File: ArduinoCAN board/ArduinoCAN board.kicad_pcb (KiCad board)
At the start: 2 copper layers, 71.1 x 58.4 mm, 8 parts, among them J1 CAN1, J2 CAN2, U1 MCP2515_board

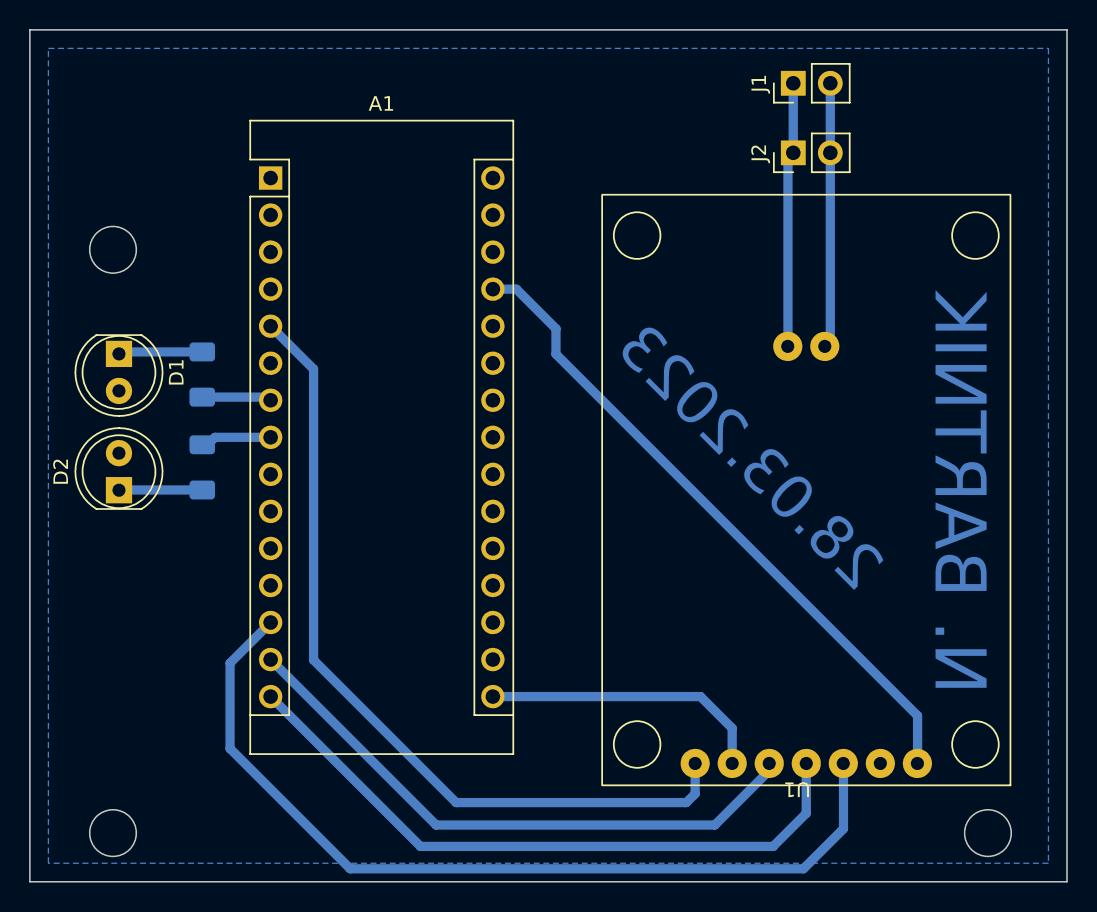
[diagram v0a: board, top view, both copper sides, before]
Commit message: added servo, pins and power connectors
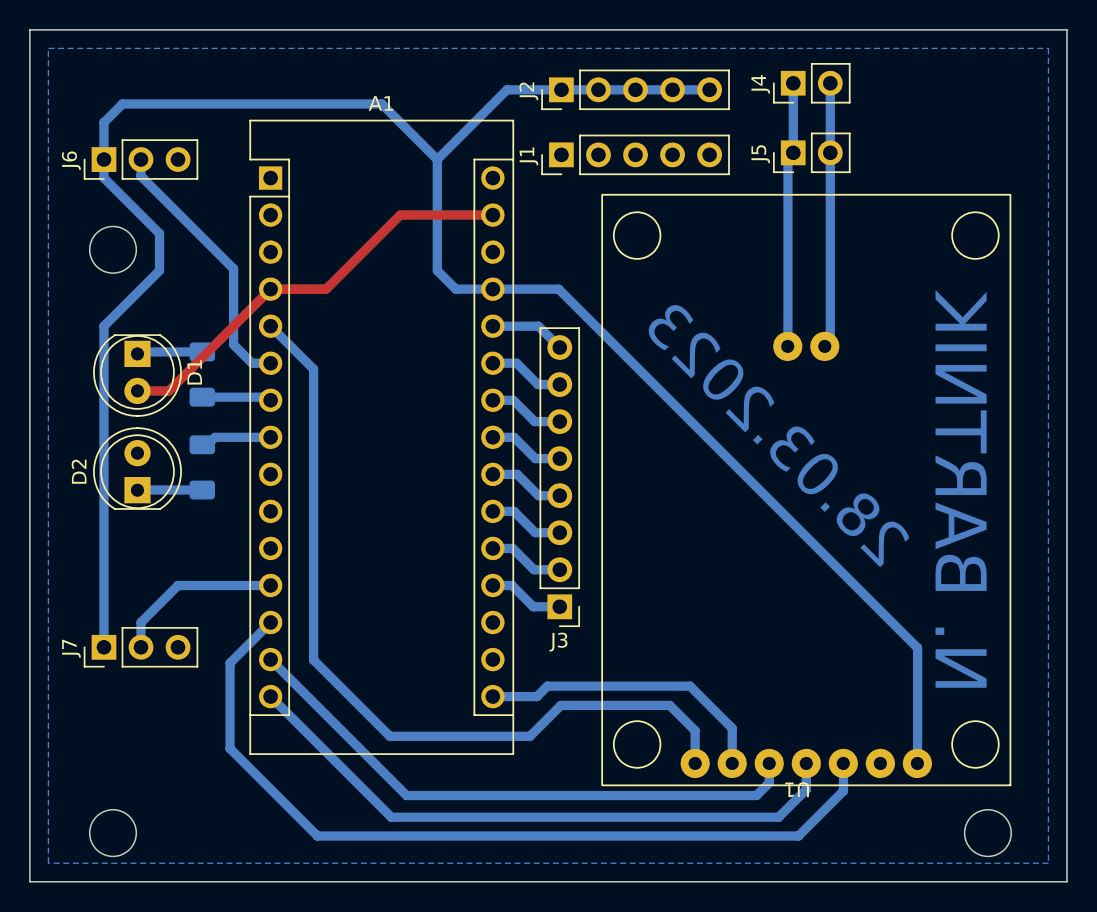
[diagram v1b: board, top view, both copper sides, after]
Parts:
- added J1: POWER, Connector_PinHeader_2.54mm:PinHeader_1x05_P2.54mm_Vertical, F.Cu at (150.8, 67.0)
- added J2: POWER, Connector_PinHeader_2.54mm:PinHeader_1x05_P2.54mm_Vertical, F.Cu at (150.8, 62.5)
- added J3: PINS, Connector_PinHeader_2.54mm:PinHeader_1x08_P2.54mm_Vertical, F.Cu at (150.6, 98.0)
- added J6: SERVO1, Connector_PinHeader_2.54mm:PinHeader_1x03_P2.54mm_Vertical, F.Cu at (119.4, 67.3)
- added J7: SERVO2, Connector_PinHeader_2.54mm:PinHeader_1x03_P2.54mm_Vertical, F.Cu at (119.4, 100.8)
- moved D1 1.27 mm to (121.7, 80.6)
- moved D2 1.27 mm to (121.7, 90.0)
- renumbered J1 to J4, J2 to J5
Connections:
- A1 pad 12: unconnected-(A1-Pad12) -> SERVO2
- A1 pad 19: unconnected-(A1-Pad19) -> Net-(A1-Pad19)
- A1 pad 20: unconnected-(A1-Pad20) -> Net-(A1-Pad20)
- A1 pad 21: unconnected-(A1-Pad21) -> Net-(A1-Pad21)
- A1 pad 22: unconnected-(A1-Pad22) -> Net-(A1-Pad22)
- A1 pad 23: unconnected-(A1-Pad23) -> Net-(A1-Pad23)
- A1 pad 24: unconnected-(A1-Pad24) -> Net-(A1-Pad24)
- A1 pad 25: unconnected-(A1-Pad25) -> Net-(A1-Pad25)
- A1 pad 26: unconnected-(A1-Pad26) -> Net-(A1-Pad26)
- A1 pad 6: unconnected-(A1-Pad6) -> SERVO1
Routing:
- net VCC: track 45.5 -> 144.0 mm
- net GND: track 0.00 -> 29.4 mm
- net SERVO1: track 0.00 -> 18.4 mm
- net SERVO2: track 0.00 -> 11.6 mm
- net Net-(A1-Pad26): track 0.00 -> 5.19 mm
- net Net-(A1-Pad25): track 0.00 -> 5.19 mm
- net Net-(A1-Pad23): track 0.00 -> 5.19 mm
- net Net-(A1-Pad21): track 0.00 -> 5.19 mm
- net Net-(A1-Pad19): track 0.00 -> 5.19 mm
- net Net-(A1-Pad24): track 0.00 -> 5.19 mm
- net Net-(A1-Pad20): track 0.00 -> 5.19 mm
- net Net-(A1-Pad22): track 0.00 -> 5.19 mm
- net CS: track 60.9 -> 57.5 mm
- net SD: track 45.3 -> 42.7 mm
- net Net-(D1-Pad1): track 5.77 -> 4.50 mm
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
